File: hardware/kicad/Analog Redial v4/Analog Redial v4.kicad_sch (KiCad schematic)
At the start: 65 parts, among them J1 Barrel_Jack_PTH_Slot, J2 PINHD_1x2_Male, J3 PINHD_1x2_Male, J4 PINHD_1x2_Male, J5 PINHD_2x4_Male, J7 PINHD_1x3_Male, J8 RJ12, J9 RJ12, U1 ESP32-C6-DevKitC-1, U2 ES8388, U3 AG1171, U4 AG1171

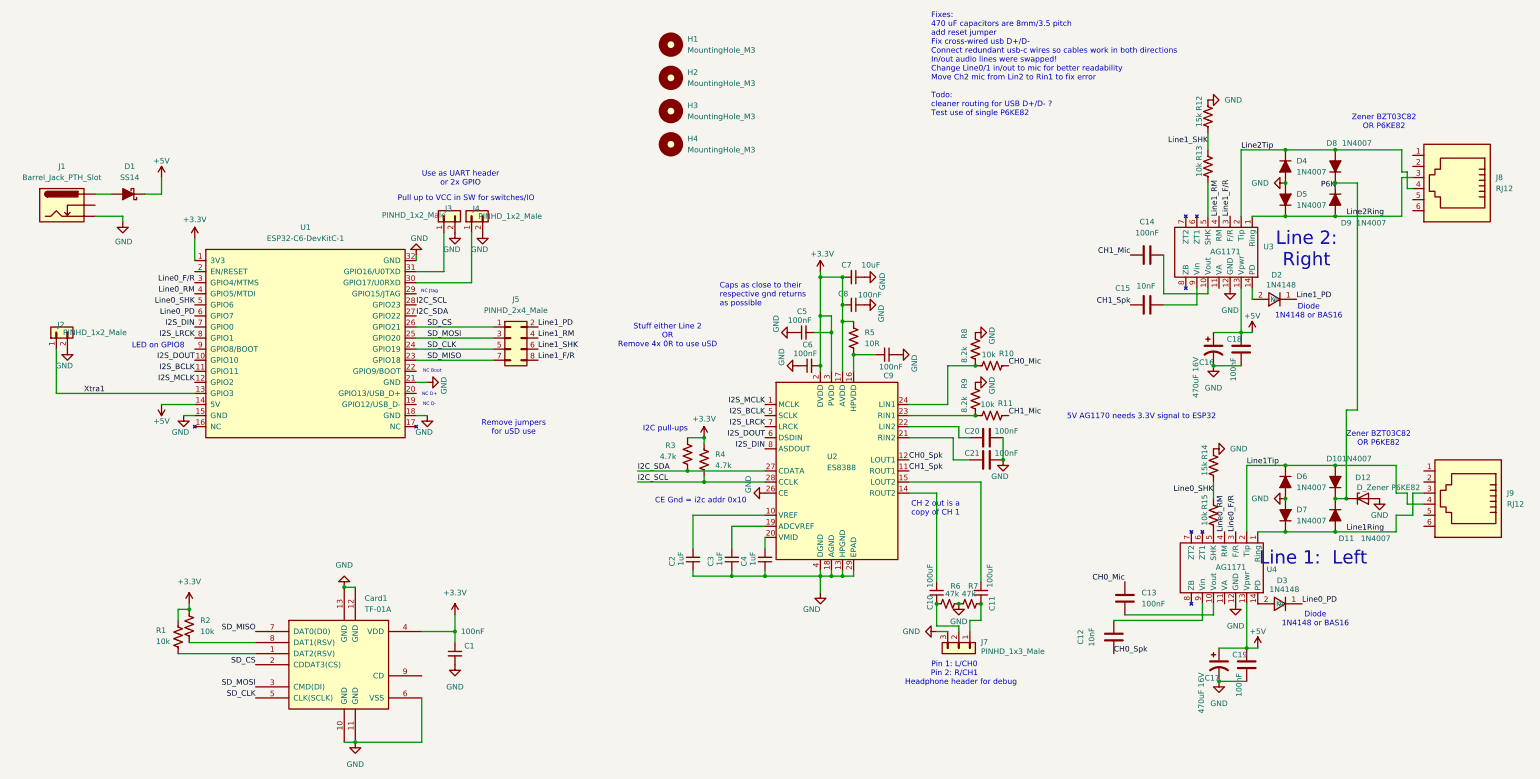
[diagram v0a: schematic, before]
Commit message: Rename KiCad projects to Analog Redial v2/v3/v4/v5
Rotary_phone_SMD2 -> "Analog Redial v2", Old/Rotary_phone_SMD3 ->
"Old/Analog Redial v3", Rotary_phone_SMD4 -> "Analog Redial v4", and
"Analog Redial 5" -> "Analog Redial v5": directories, project files, and the
project-name references inside them (schematic annotation instances, the
PCB's sheet-file fields), checked by exporting each netlist -- every part is
still annotated. Silkscreen text and the SMD2 Gerber outputs keep their
names. Doc and code references updated (link targets URL-encoded); two
already-broken SMD2 BOM CSV links fixed on the way.

Firmware board-type names (CONFIG_BOARD_TYPE_SMD2/SMD4/SMD5) unchanged.

Co-Authored-By: Claude Opus 5.5 <noreply@anthropic.com>
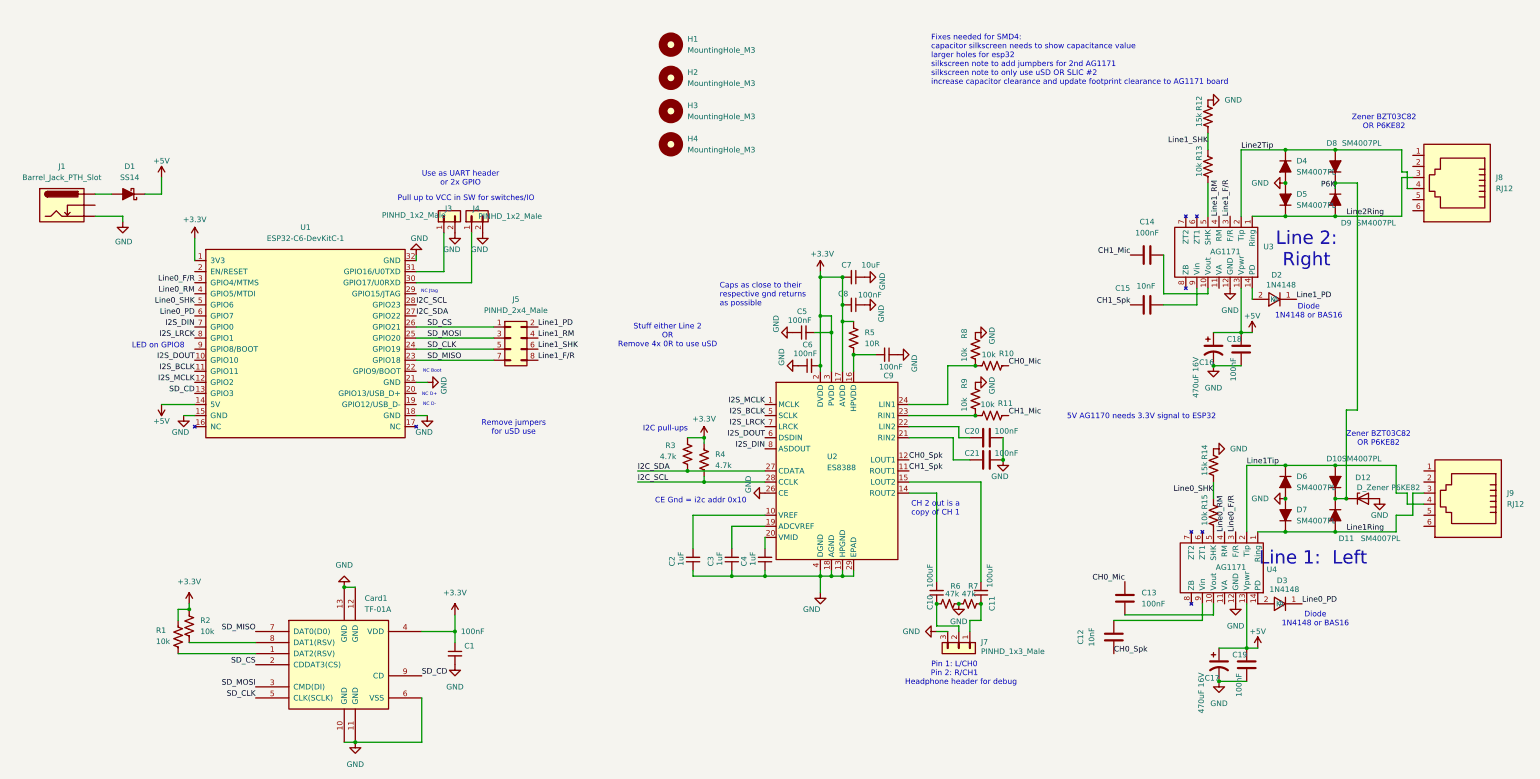
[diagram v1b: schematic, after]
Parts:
- removed J2: PINHD_1x2_Male, Connector_PinHeader_2.54mm:PinHeader_1x02_P2.54mm_Vertical, symbol PCM_SL_Pin_Headers:PINHD_1x2_Male
- D10, D11, D4, D5, D6, D7, D8, D9: value 1N4007 -> SM4007PL; footprint JLCImport:1N4007W_C18199088 -> Diode_SMD:Nexperia_CFP3_SOD-123W
- R8, R9: value 8.2k -> 10k
- U3, U4: symbol Custom_Symbol_Library:AG1171_SIL -> Custom:AG1171_SIL
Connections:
- net Xtra1 is gone; now on net SD_CD: U1.13 (GPIO3)
- net SD_CD: now reaches Card1.9 (CD)
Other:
- note added: "Fixes needed for SMD4: capacitor silkscreen needs to show capacitance value larger holes for esp32 silkscreen note to add jumpbers for 2nd AG1171 silkscreen note to only use uSD OR SLIC #2 increase capacitor clearance and update footprint clearance to AG1171 board"
- note removed: "Fixes: 470 uF capacitors are 8mm/3.5 pitch add reset jumper Fix cross-wired usb D+/D- Connect redundant usb-c wires so cables work in both directions In/out audio lines were swapped! Change Line0/1 in/out to mic for better readability Move Ch2 mic from Lin2 to Rin1 to fix error Todo: cleaner routing for USB D+/D- ? Test use of single P6KE82"
